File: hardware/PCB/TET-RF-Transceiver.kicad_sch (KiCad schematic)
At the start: 26 parts, among them U11 SMA_1, U12 W25Q128JVSIQTR, U13 W25Q128JVSIQTR, U14 E80-900M2213S, U15 SMA_2, U16 W25Q128JVSIQTR, U17 TMP112AIDRLR, U18 INA226AQDGSRQ1, U19 TMP112AIDRLR

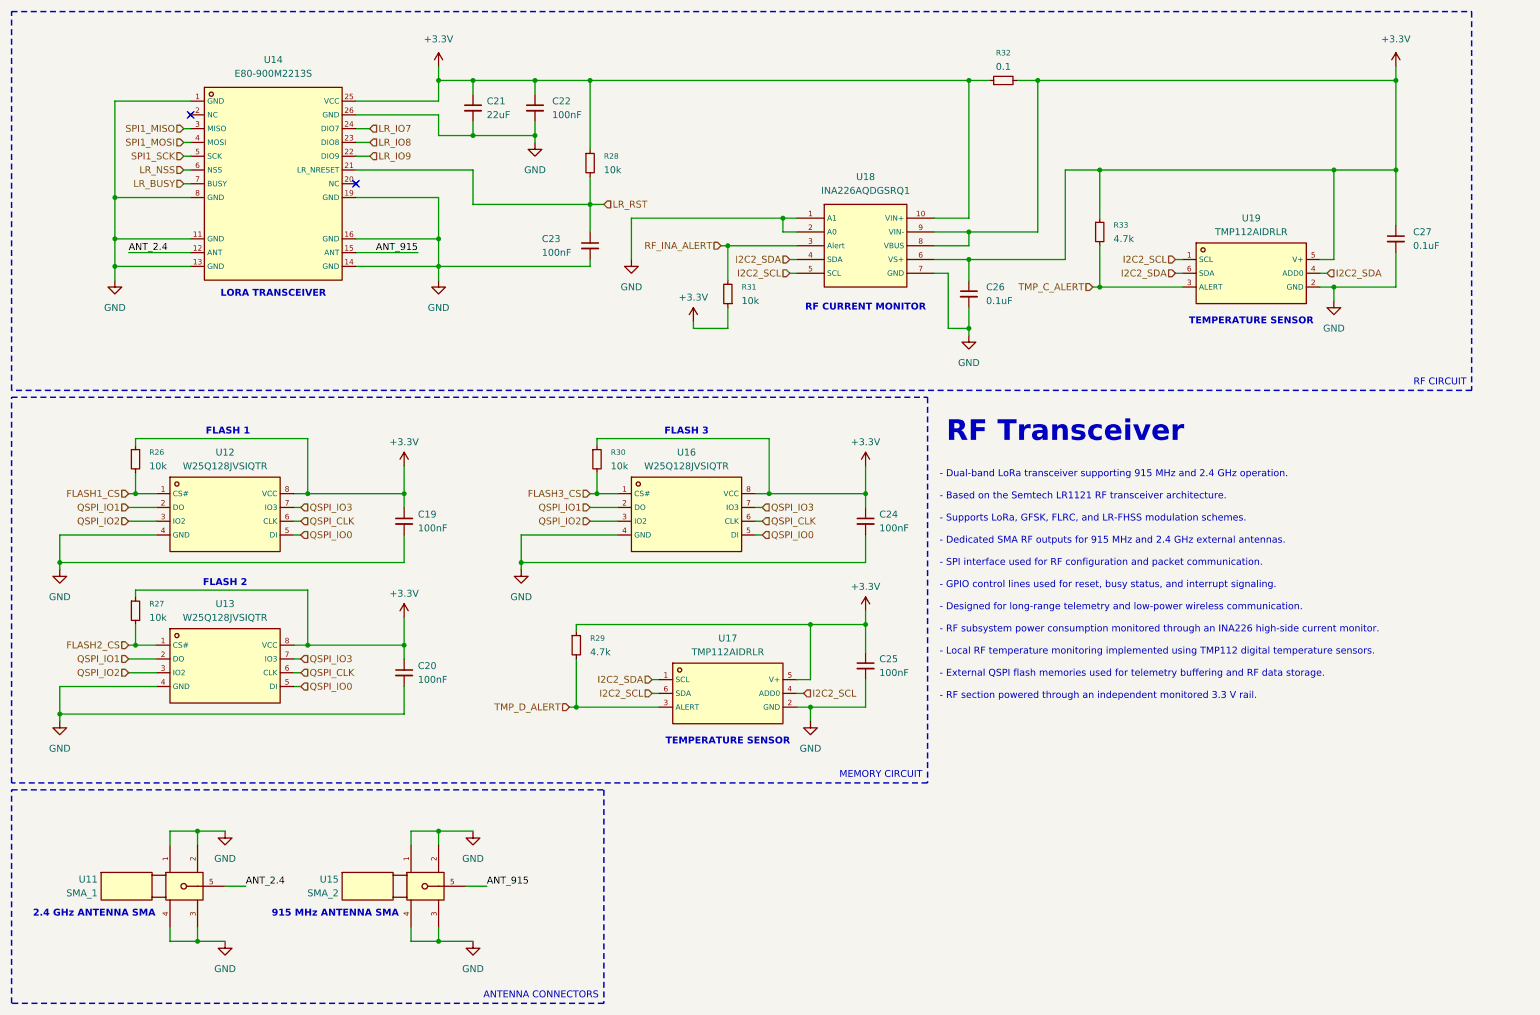
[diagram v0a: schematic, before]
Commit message: feat(hardware): implement TET module PCB design and restructure project
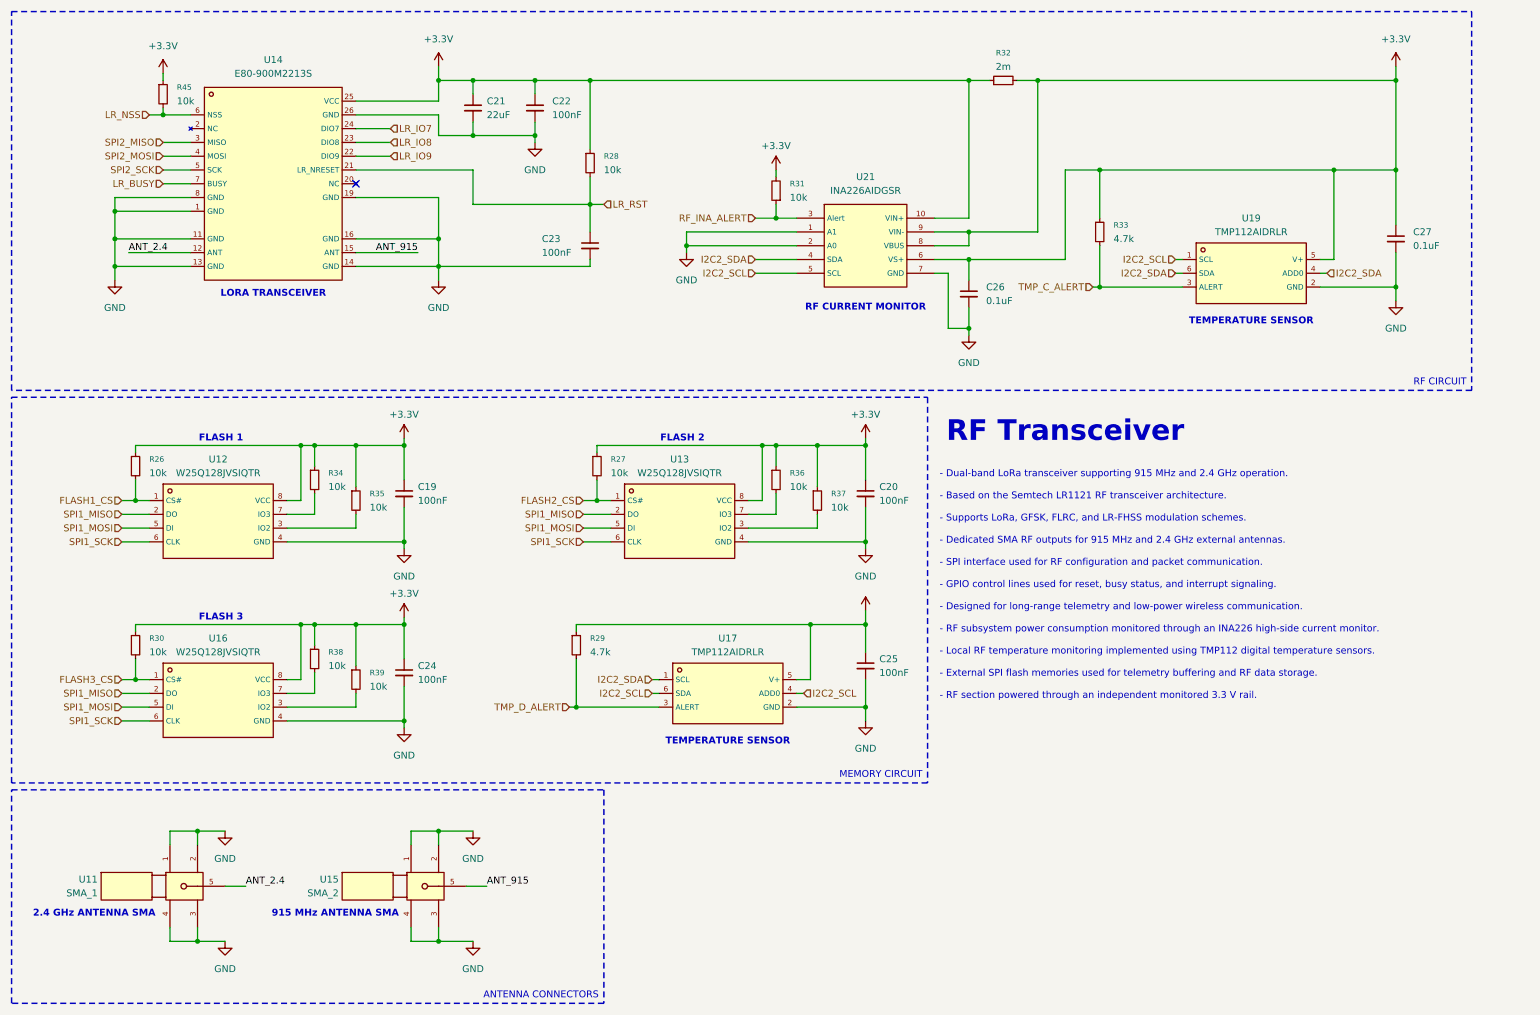
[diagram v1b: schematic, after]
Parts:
- removed U18: INA226AQDGSRQ1, TET-Footprints:VSSOP-10_L3.0-W3.0-P0.50-LS4.9-BL, symbol TET-Symbols:INA226AQDGSRQ1
- added R34, R35, R36, R37, R38, R39, R45: 10k, Resistor_SMD:R_0402_1005Metric, symbol Device:R_Small
- added U21: INA226AIDGSR, TET-Footprints:MSOP-10_L3.0-W3.0-P0.50-LS5.0-BL, symbol TET-Symbols:INA226AIDGSR
- C19, C20, C21, C22, C23, C24, C25, C26, C27: footprint Capacitor_SMD:C_0603_1608Metric -> Capacitor_SMD:C_0402_1005Metric
- R26, R27, R28, R29, R30, R31, R33: footprint Resistor_SMD:R_0603_1608Metric -> Resistor_SMD:R_0402_1005Metric
- R32: value 0.1 -> 2m; footprint Resistor_SMD:R_1206_3216Metric -> TET-Footprints:RES-SMD_L6.3-W3.1-1
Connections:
- net QSPI_CLK is gone; now on net SPI1_SCK: U12.6 (CLK), U13.6 (CLK), U16.6 (CLK)
- net QSPI_IO0 is gone; now on net SPI1_MOSI: U12.5 (DI), U13.5 (DI), U16.5 (DI)
- net QSPI_IO1 is gone; now on net SPI1_MISO: U12.2 (DO), U13.2 (DO), U16.2 (DO)
- net +3.3V: now also R31.2, R34.1, R35.1, R36.1, R37.1, R38.1, R39.1, R45.1, U21.10 (VIN+), U21.6 (VS+), U21.8 (VBUS), U21.9 (VIN-); no longer R31.1
- net GND: now also U21.1 (A1), U21.2 (A0), U21.7 (GND)
- net I2C2_SCL: now also U21.5 (SCL)
- net I2C2_SDA: now also U21.4 (SDA)
- net LR_NSS: now also R45.2
- net RF_INA_ALERT: now also R31.1, U21.3 (Alert); no longer R31.2
- net SPI1_MISO: no longer U14.3 (MISO)
- net SPI1_MOSI: no longer U14.4 (MOSI)
- net SPI1_SCK: no longer U14.5 (SCK)
- removed net QSPI_IO2: U12.3 (IO2), U13.3 (IO2), U16.3 (IO2)
- removed net QSPI_IO3: U12.7 (IO3), U13.7 (IO3), U16.7 (IO3)
- new net: R34.2, U12.7 (IO3)
- new net: R37.2, U13.3 (IO2)
- new net: R39.2, U16.3 (IO2)
- new net: R38.2, U16.7 (IO3)
- new net: R35.2, U12.3 (IO2)
- new net: R36.2, U13.7 (IO3)
- new net SPI2_MISO: U14.3 (MISO)
- new net SPI2_MOSI: U14.4 (MOSI)
- new net SPI2_SCK: U14.5 (SCK)
- no-connect marks 2 -> 1
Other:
- moved on the sheet: C19, R26, R31, U12

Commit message: feat(hardware): complete PCB layout and project structure
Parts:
- C21: footprint Capacitor_SMD:C_0402_1005Metric -> Capacitor_SMD:C_0805_2012Metric
- C26, C27: value 0.1uF -> 100nF
- R32: LCSC (none) -> C695817
- U11: value SMA_1 -> SMA
- U15: value SMA_2 -> SMA
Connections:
- net +3.3V: no longer C21.1, C22.1, R28.1, R32.1, U14.25 (VCC), U21.10 (VIN+)
- new net RF_LOAD: C21.1, C22.1, R28.1, R32.1, U14.25 (VCC), U21.10 (VIN+)
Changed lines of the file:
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@@
 	(title_block
 		(title "TET Module")
-		(date "2026-05-01")
-		(rev "1.0")
+		(date "2026-06-09")
+		(rev "v1r1")
 		(company "ICDT")
-		(comment 1 "PCB-01")
+		(comment 1 "TET-v1r1")
 		(comment 2 "Rodrigo Andrade")
-		(comment 3 "01/05/2026")
+		(comment 3 "09/06/2026")
 	)
 	(text "TEMPERATURE SENSOR"
@@
 	)
 	(junction
+		(at 140.97 26.67)
+		(diameter 0)
+		(color 0 0 0 0)
+	)
+	(junction
 		(at 269.24 26.67)
 		(diameter 0)
@@
 	)
 	(junction
-		(at 92.71 26.67)
-		(diameter 0)
-		(color 0 0 0 0)
-	)
-	(junction
 		(at 162.56 93.98)
 		(diameter 0)
@@
 	(wire
 		(pts
-			(xy 92.71 24.13) (xy 92.71 26.67)
-		)
-		(stroke
-			(width 0)
-			(type default)
-		)
-	)
-	(wire
-		(pts
 			(xy 97.79 175.26) (xy 101.6 175.26)
 		)
@@
 	(wire
 		(pts
-			(xy 120.65 26.67) (xy 190.5 26.67)
+			(xy 120.65 26.67) (xy 140.97 26.67)
 		)
 		(stroke
@@
 	(wire
 		(pts
+			(xy 140.97 25.4) (xy 140.97 26.67)
+		)
+		(stroke
+			(width 0)
+			(type default)
+		)
+	)
+	(wire
+		(pts
 			(xy 99.06 185.42) (xy 92.71 185.42)
 		)
@@
 	(wire
 		(pts
+			(xy 140.97 26.67) (xy 190.5 26.67)
+		)
+		(stroke
+			(width 0)
+			(type default)
+		)
+	)
+	(wire
+		(pts
 			(xy 214.63 43.18) (xy 257.81 43.18)
 		)
@@
 		)
 	)
+	(label "RF_LOAD"
+		(at 153.67 26.67 0)
+		(effects
+			(font
+				(size 1.27 1.27)
+			)
+			(justify left bottom)
+		)
+	)
 	(label "ANT_915"
 		(at 88.9 58.42 180)
@@
 			)
 		)
-		(property "Datasheet" ""
+		(property "Datasheet" "https://www.lcsc.com/datasheet/C695817.pdf"
 			(at 196.85 26.67 0)
 			(hide yes)
@@
 			)
 		)
+		(property "LCSC" "C695817"
+			(at 196.85 26.67 90)
+			(hide yes)
+			(show_name no)
+			(do_not_autoplace no)
+			(effects
+				(font
+					(size 1.27 1.27)
+				)
+			)
+		)
 		(pin "2"
 		)
@@
 			)
 		)
-		(property "Footprint" "Capacitor_SMD:C_0402_1005Metric"
+		(property "Footprint" "Capacitor_SMD:C_0805_2012Metric"
 			(at 99.06 31.75 0)
 			(hide yes)
@@
 			)
 		)
-		(property "Datasheet" "https://item.szlcsc.com/221388.html"
+		(property "Datasheet" "https://www.ti.com/lit/ds/symlink/ina226.pdf"
 			(at 154.432 68.834 0)
 			(hide yes)
@@
 	)
 	(symbol
-		(lib_id "power:+3.3V")
-		(at 92.71 24.13 0)
-		(unit 1)
-		(body_style 1)
-		(exclude_from_sim no)
-		(in_bom yes)
-		(on_board yes)
-		(in_pos_files yes)
-		(dnp no)
-		(fields_autoplaced yes)
-		(property "Reference" "#PWR053"
-			(at 92.71 27.94 0)
-			(hide yes)
-			(show_name no)
-			(do_not_autoplace no)
-			(effects
-				(font
-					(size 1.27 1.27)
-				)
-			)
-		)
-		(property "Value" "+3.3V"
-			(at 92.71 19.05 0)
-			(show_name no)
-			(do_not_autoplace no)
-			(effects
-				(font
-					(size 1.27 1.27)
-				)
-			)
-		)
-		(property "Footprint" ""
-			(at 92.71 24.13 0)
-			(hide yes)
-			(show_name no)
-			(do_not_autoplace no)
-			(effects
-				(font
-					(size 1.27 1.27)
-				)
-			)
-		)
-		(property "Datasheet" ""
-			(at 92.71 24.13 0)
-			(hide yes)
-			(show_name no)
-			(do_not_autoplace no)
-			(effects
-				(font
-					(size 1.27 1.27)
-				)
-			)
-		)
-		(property "Description" "Power symbol creates a global label with name \"+3.3V\""
-			(at 92.71 24.13 0)
-			(hide yes)
-			(show_name no)
-			(do_not_autoplace no)
-			(effects
-				(font
-					(size 1.27 1.27)
-				)
-			)
-		)
-		(pin "1"
-		)
-		(instances
-			(project "TET"
-				(path "/9ad3bc3a-e567-4764-b6aa-630c8b7f3c7b/64ee994d-a0f8-4131-90b0-8a68ffe29a18"
-					(reference "#PWR053")
-					(unit 1)
-				)
-			)
-		)
-	)
-	(symbol
 		(lib_id "power:GND")
 		(at 138.43 58.42 0)
@@
 			)
 		)
-		(property "Value" "SMA_2"
+		(property "Value" "SMA"
 			(at 74.295 176.5299 0)
 			(show_name no)
@@
 			)
 		)
-		(property "Value" "SMA_1"
+		(property "Value" "SMA"
 			(at 29.845 176.5299 0)
 			(show_name no)
@@
 		(fields_autoplaced yes)
 		(property "Reference" "C27"
-			(at 272.415 54.6162 0)
+			(at 271.78 54.6162 0)
 			(show_name no)
 			(do_not_autoplace no)
@@
 			)
 		)
-		(property "Value" "0.1uF"
-			(at 272.415 57.1562 0)
+		(property "Value" "100nF"
+			(at 271.78 57.1562 0)
 			(show_name no)
 			(do_not_autoplace no)
@@
 	)
 	(symbol
+		(lib_id "power:PWR_FLAG")
+		(at 140.97 25.4 0)
+		(unit 1)
+		(body_style 1)
+		(exclude_from_sim no)
+		(in_bom yes)
+		(on_board yes)
+		(in_pos_files yes)
+		(dnp no)
+		(fields_autoplaced yes)
+		(property "Reference" "#FLG01"
+			(at 140.97 23.495 0)
+			(hide yes)
+			(show_name no)
+			(do_not_autoplace no)
+			(effects
+				(font
+					(size 1.27 1.27)
+				)
+			)
+		)
+		(property "Value" "PWR_FLAG"
+			(at 140.97 20.32 0)
+			(show_name no)
+			(do_not_autoplace no)
+			(effects
+				(font
+					(size 1.27 1.27)
+				)
+			)
+		)
+		(property "Footprint" ""
+			(at 140.97 25.4 0)
+			(hide yes)
+			(show_name no)
+			(do_not_autoplace no)
+			(effects
+				(font
+					(size 1.27 1.27)
+				)
+			)
+		)
+		(property "Datasheet" ""
+			(at 140.97 25.4 0)
+			(hide yes)
+			(show_name no)
+			(do_not_autoplace no)
+			(effects
+				(font
+					(size 1.27 1.27)
+				)
+			)
+		)
+		(property "Description" "Special symbol for telling ERC where power comes from"
+			(at 140.97 25.4 0)
+			(hide yes)
+			(show_name no)
+			(do_not_autoplace no)
+			(effects
+				(font
+					(size 1.27 1.27)
+				)
+			)
+		)
+		(pin "1"
+		)
+		(instances
+			(project "TET"
+				(path "/9ad3bc3a-e567-4764-b6aa-630c8b7f3c7b/64ee994d-a0f8-4131-90b0-8a68ffe29a18"
+					(reference "#FLG01")
+					(unit 1)
+				)
+			)
+		)
+	)
+	(symbol
 		(lib_id "power:GND")
 		(at 33.02 63.5 0)
@@
 		(fields_autoplaced yes)
 		(property "Reference" "C26"
-			(at 193.675 64.7762 0)
+			(at 193.04 64.7762 0)
 			(show_name no)
 			(do_not_autoplace no)
@@
 			)
 		)
-		(property "Value" "0.1uF"
-			(at 193.675 67.3162 0)
+		(property "Value" "100nF"
+			(at 193.04 67.3162 0)
 			(show_name no)
 			(do_not_autoplace no)
